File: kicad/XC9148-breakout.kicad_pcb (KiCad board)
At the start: 2 copper layers, 24.2 x 16.7 mm, 7 parts, among them IC1 XC9148G50CER-G, J3 Conn_01x03, J4 Conn_01x02

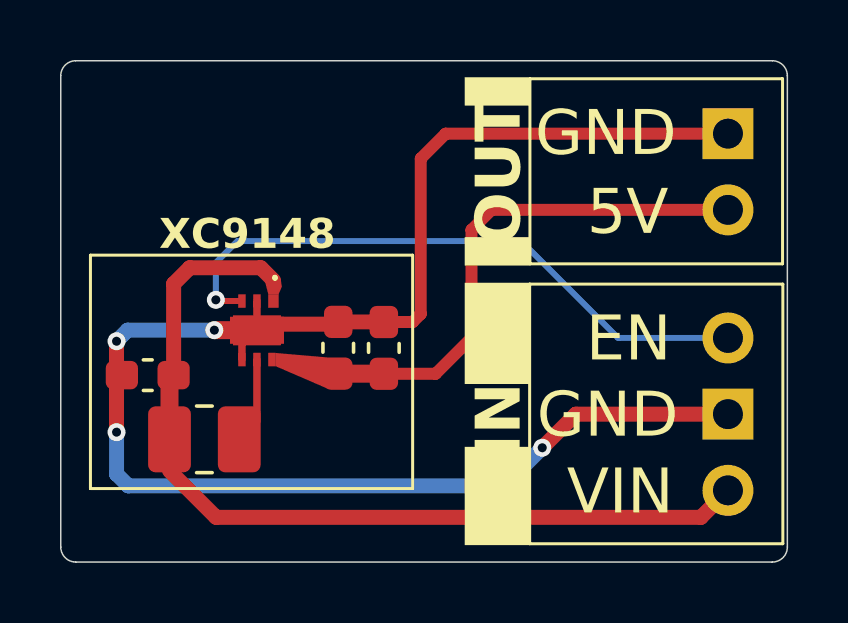
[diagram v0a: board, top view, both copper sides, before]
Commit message: update XC9148 footprint for easier soldering by hand
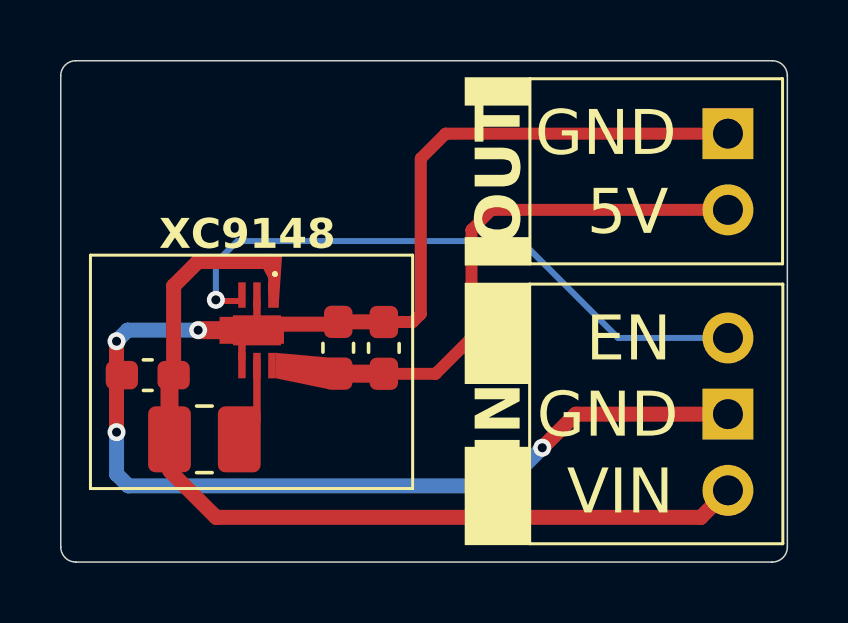
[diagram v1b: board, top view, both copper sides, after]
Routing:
- net IN: track 30.1 -> 31.0 mm
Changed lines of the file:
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@@
 			(drillshape 0)
 			(scaleselection 1)
-			(outputdirectory "gerbers/")
+			(outputdirectory "../gerbers/")
 		)
 	)
@@
 		(attr smd)
 		(fp_line
-			(start -1.8 -0.6)
-			(end -1.8 -0.6)
+			(start -1.924632 -0.600349)
+			(end -1.924632 -0.600349)
 			(stroke
 				(width 0.1)
@@
 		)
 		(fp_line
-			(start -1.7 -0.6)
-			(end -1.7 -0.6)
+			(start -1.824632 -0.600349)
+			(end -1.824632 -0.600349)
 			(stroke
 				(width 0.1)
@@
 		)
 		(fp_arc
-			(start -1.8 -0.6)
-			(mid -1.75 -0.65)
-			(end -1.7 -0.6)
+			(start -1.924632 -0.600349)
+			(mid -1.874632 -0.650349)
+			(end -1.824632 -0.600349)
 			(stroke
 				(width 0.1)
@@
 		)
 		(fp_arc
-			(start -1.7 -0.6)
-			(mid -1.75 -0.55)
-			(end -1.8 -0.6)
+			(start -1.824632 -0.600349)
+			(mid -1.874632 -0.550349)
+			(end -1.924632 -0.600349)
 			(stroke
 				(width 0.1)
@@
 		)
 		(pad "1" smd rect
-			(at -0.975 -0.55)
-			(size 0.35 0.45)
+			(at -1.175 -0.55)
+			(size 0.35 0.85)
 			(layers "F.Cu" "F.Paste" "F.Mask")
 			(net 1 "IN")
@@
 		)
 		(pad "2" smd rect
-			(at -0.975 0)
-			(size 0.25 0.45)
+			(at -1.175 0)
+			(size 0.25 0.85)
 			(layers "F.Cu" "F.Paste" "F.Mask")
 			(net 2 "GND")
@@
 		)
 		(pad "3" smd rect
-			(at -0.975 0.5)
-			(size 0.25 0.45)
+			(at -1.175 0.5)
+			(size 0.25 0.85)
 			(layers "F.Cu" "F.Paste" "F.Mask")
 			(net 5 "ENABLE")
@@
 		)
 		(pad "4" smd rect
-			(at 0.975 0.5)
-			(size 0.25 0.45)
+			(at 1.175 0.5)
+			(size 0.25 0.85)
 			(layers "F.Cu" "F.Paste" "F.Mask")
 			(net 2 "GND")
@@
 		)
 		(pad "5" smd rect
-			(at 0.975 0)
-			(size 0.25 0.45)
+			(at 1.175 0)
+			(size 0.25 0.85)
 			(layers "F.Cu" "F.Paste" "F.Mask")
 			(net 4 "LX")
@@
 		)
 		(pad "6" smd rect
-			(at 0.975 -0.5)
-			(size 0.25 0.45)
+			(at 1.175 -0.5)
+			(size 0.25 0.85)
 			(layers "F.Cu" "F.Paste" "F.Mask")
 			(net 3 "OUT")
@@
 		(pad "9" smd rect
 			(at 0 0.85)
-			(size 0.1 0.9)
+			(size 0.8 0.9)
 			(layers "F.Cu" "F.Paste" "F.Mask")
 			(net 2 "GND")
@@
 	(gr_poly
 		(pts
-			(xy 102.09 60.1) (xy 101.98 59.68) (xy 102.38 59.41) (xy 102.5 59.57) (xy 102.54 59.84) (xy 102.43 60.1)
+			(xy 102.382299 60.492935) (xy 102.5 58.800889) (xy 101.75 58.801557) (xy 102.24653 59.762059)
 		)
 		(stroke
-			(width 0.001)
+			(width 0.1)
 			(type solid)
 		)
@@
 	(gr_poly
 		(pts
-			(xy 102.33 62.05) (xy 104.18 62.21) (xy 104.11 63.26) (xy 102.33 62.49)
+			(xy 102.32938 62.045175) (xy 104.18 62.21) (xy 104.11 63.26) (xy 102.322272 62.890037)
 		)
 		(stroke
@@
 	)
 	(segment
-		(start 101.84 59.21)
-		(end 102.26 59.63)
-		(width 0.5)
-		(layer "F.Cu")
-		(net 1)
-	)
-	(segment
-		(start 99.47 59.21)
-		(end 101.84 59.21)
-		(width 0.5)
-		(layer "F.Cu")
-		(net 1)
-	)
-	(segment
 		(start 98.795 64.93)
 		(end 98.795 62.9275)
@@
 	)
 	(segment
-		(start 98.9325 59.7475)
-		(end 99.47 59.21)
-		(width 0.5)
-		(layer "F.Cu")
-		(net 1)
-	)
-	(segment
 		(start 102.29 60.29)
 		(end 102.26 60.32)
@@
 	)
 	(segment
+		(start 102.26 59.01)
+		(end 102.25 59)
+		(width 0.2)
+		(layer "F.Cu")
+		(net 1)
+	)
+	(segment
+		(start 98.9325 62.79)
+		(end 98.9325 59.8175)
+		(width 0.5)
+		(layer "F.Cu")
+		(net 1)
+	)
+	(segment
 		(start 116.51 67.53)
 		(end 117.41 66.63)
@@
 	)
 	(segment
+		(start 102.26 60.045)
+		(end 102.26 59.01)
+		(width 0.35)
+		(layer "F.Cu")
+		(net 1)
+	)
+	(segment
+		(start 99.75 59)
+		(end 102.25 59)
+		(width 0.5)
+		(layer "F.Cu")
+		(net 1)
+	)
+	(segment
 		(start 98.795 64.93)
 		(end 98.795 65.975)
@@
 	)
 	(segment
-		(start 98.9325 62.79)
-		(end 98.9325 59.7475)
-		(width 0.5)
-		(layer "F.Cu")
-		(net 1)
-	)
-	(segment
 		(start 117.41 66.63)
 		(end 117.38 66.63)
@@
 	)
 	(segment
+		(start 98.9325 59.8175)
+		(end 99.75 59)
+		(width 0.5)
+		(layer "F.Cu")
+		(net 1)
+	)
+	(segment
+		(start 99.75 61.29)
+		(end 101.705 61.29)
+		(width 0.6)
+		(layer "F.Cu")
+		(net 2)
+	)
+	(segment
 		(start 97.03 62.9675)
 		(end 97.2075 62.79)
@@
 	)
 	(segment
-		(start 100.29 61.29)
-		(end 101.705 61.29)
-		(width 0.6)
-		(layer "F.Cu")
-		(net 2)
-	)
-	(segment
 		(start 104.42 61.015)
 		(end 105.935 61.015)
@@
 	)
 	(via
-		(at 100.29 61.29)
+		(at 99.75 61.29)
 		(size 0.6)
 		(drill 0.3)
@@
 	)
 	(segment
+		(start 99.75 61.29)
+		(end 97.4 61.29)
+		(width 0.5)
+		(layer "B.Cu")
+		(net 2)
+	)
+	(segment
 		(start 97.4 61.29)
-		(end 100.29 61.29)
+		(end 97.03 61.66)
 		(width 0.5)
 		(layer "B.Cu")
@@
 		(width 0.5)
 		(layer "B.Cu")
-		(net 2)
-	)
-	(segment
-		(start 97.03 61.66)
-		(end 97.4 61.29)
-		(width 0.5)
-		(layer "B.Cu")
